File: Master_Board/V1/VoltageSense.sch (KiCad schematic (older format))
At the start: 35 parts, among them J801 649002227222, J802 649002227222, J803 649002227222, J804 649002227222, U801 ACPL-C87A-500E, U802 NCS1S2405SC, U803 ACPL-C87A-500E, U804 LMV321RILT, U805 LMV321RILT

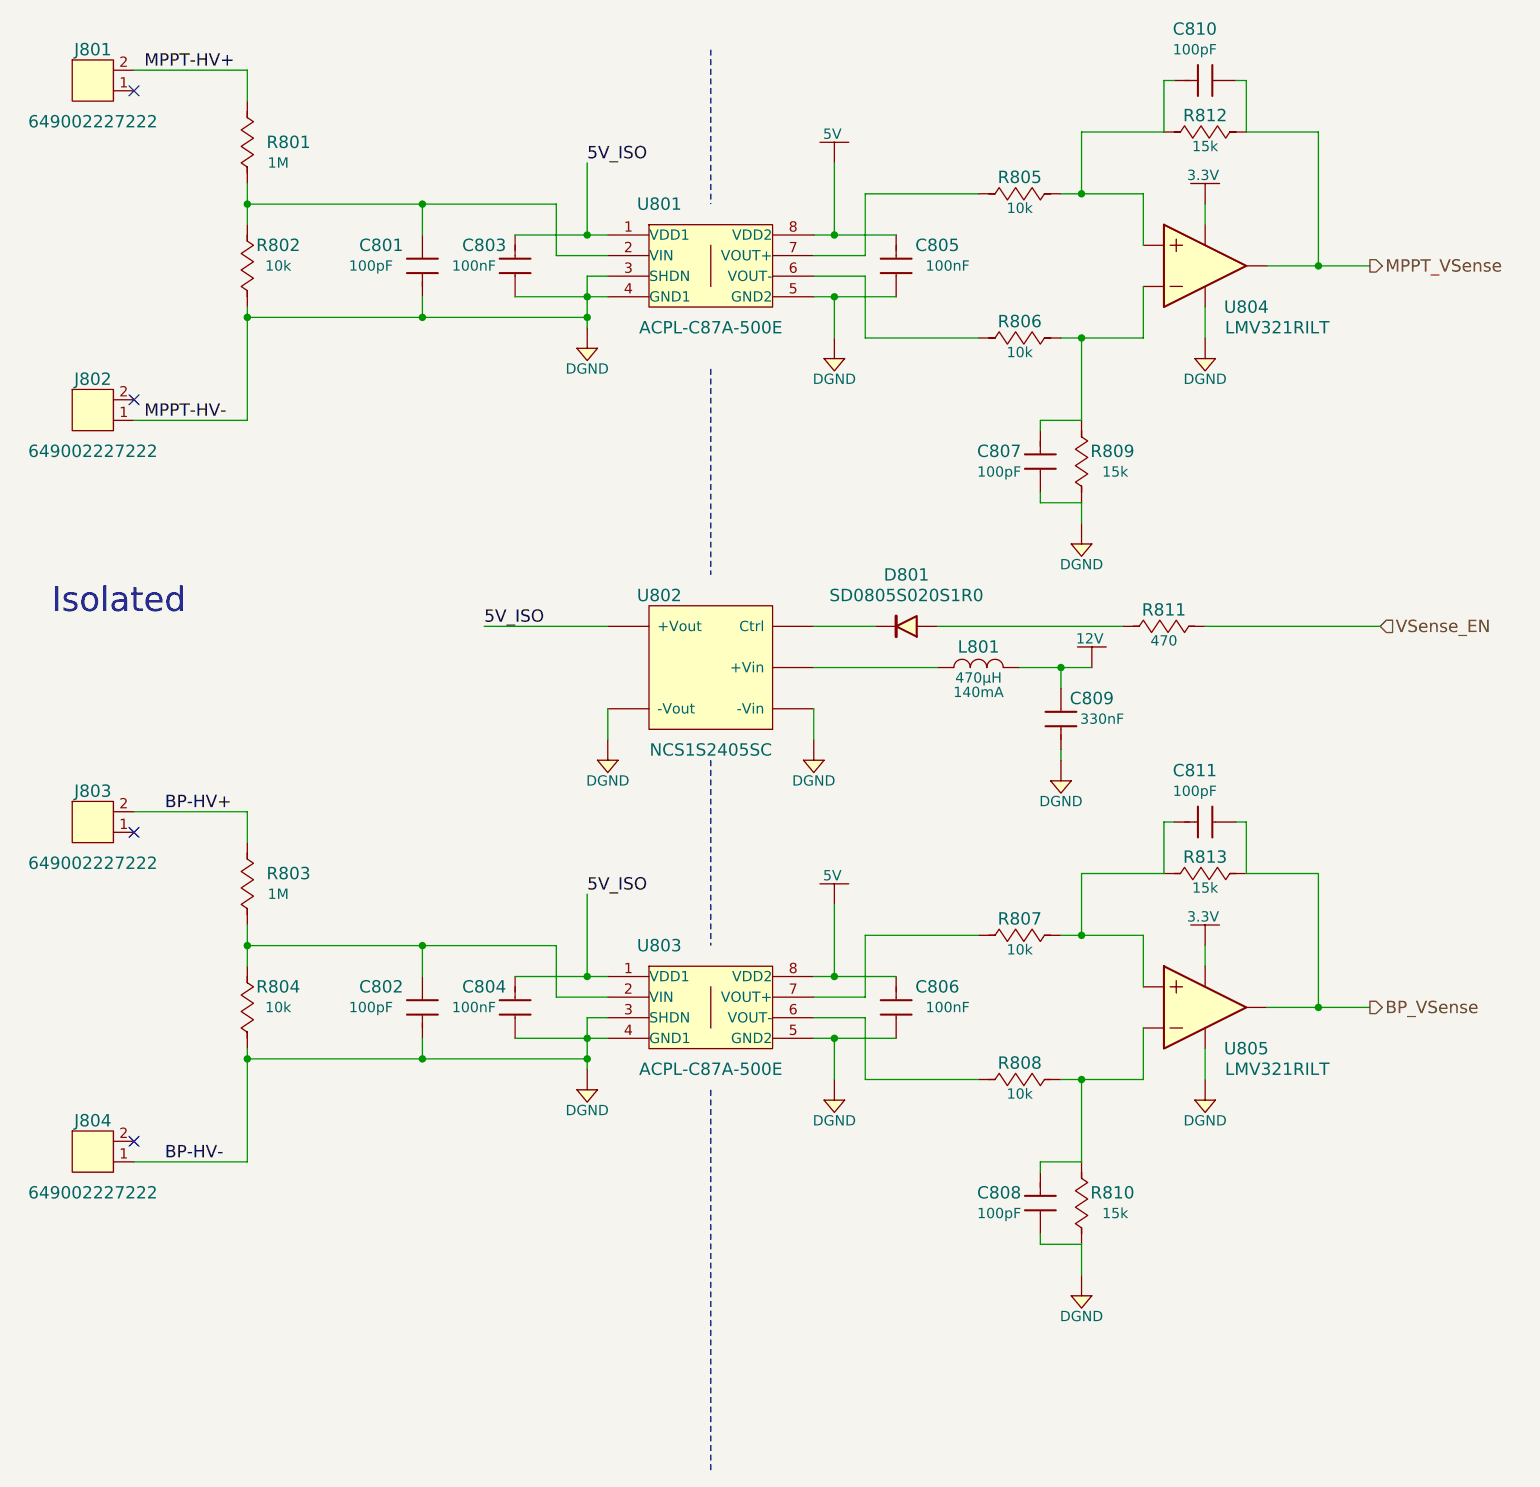
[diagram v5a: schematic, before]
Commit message: Create Master board PCB
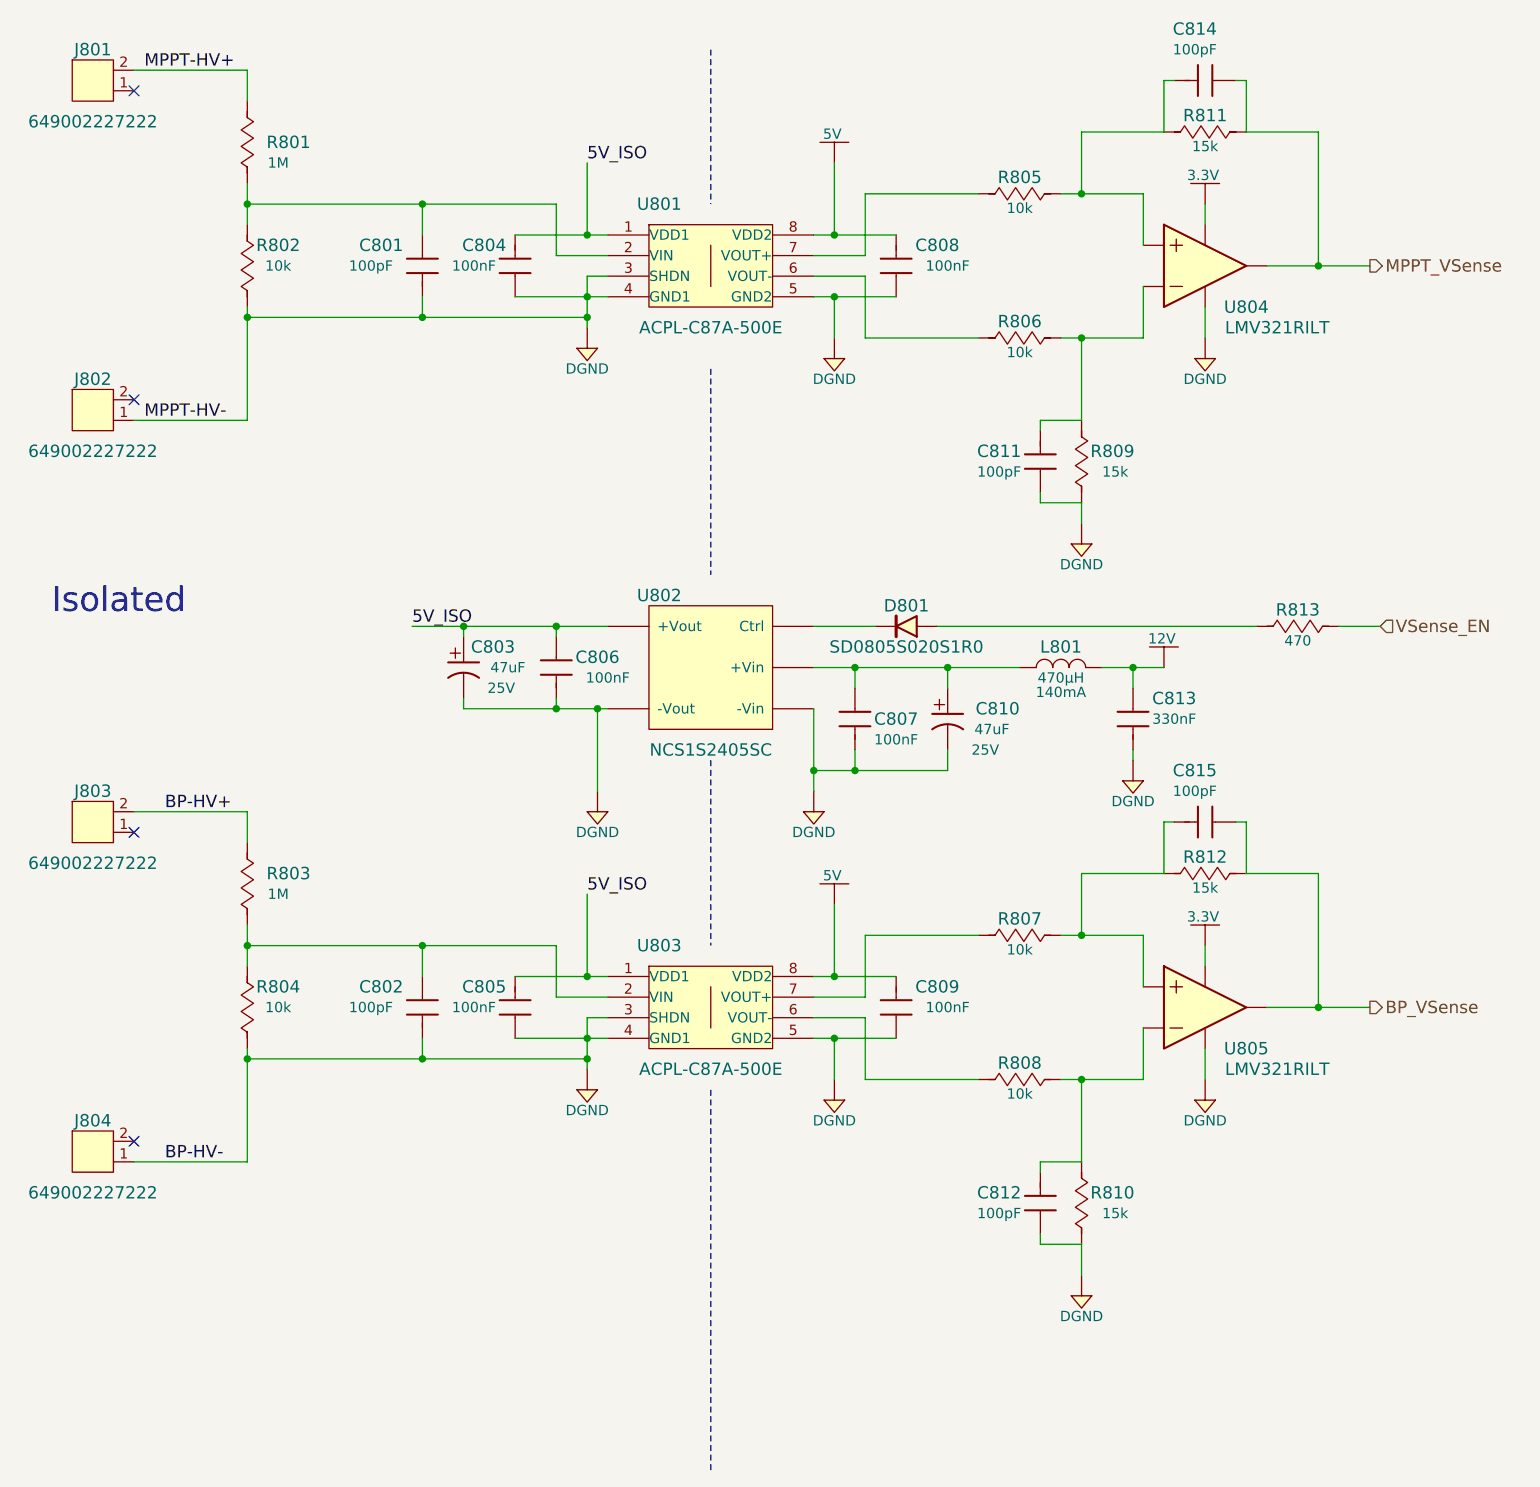
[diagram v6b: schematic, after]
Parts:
- removed L801: RLB0608-471KL, Inductors:RLB0608, symbol RLB0608-471KL
- added C803, C810: 860020472006, Capacitors:Radial-Can-5_11_2, symbol 860020472006
- added C806, C807: 885012207098, Capacitors:C0805, symbol 885012207098
- added L801: 744052471, Inductors:WE-TPC-SMD, symbol 744052471
- renumbered C803 to C804, C804 to C805, C805 to C808, C806 to C809, C807 to C811, C808 to C812, C809 to C813, C810 to C814, C811 to C815, R812 to R811, R813 to R812, R811 to R813
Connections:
- net 12V: now also L801.2
- net 5V_ISO: now also C803.1 (Positif), C806.1
- net DGND: now also C803.2 (Negatif), C806.2, C807.2, C810.2 (Negatif)
- net at U802.2 (+Vin): now also C807.1, C810.1 (Positif), L801.1
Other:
- moved on the sheet: C813, R813

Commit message: Modify Master_board PCB
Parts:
- U802: footprint IC:MSOP-8-EP -> IC:NCS1S2405SC
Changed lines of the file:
@@
 encoding utf-8
 Sheet 8 11
-Title ""
-Date ""
-Rev ""
-Comp ""
-Comment1 ""
+Title "Voltage Sense"
+Date "2017-06-25"
+Rev "V1"
+Comp "Eclipse Solar Car"
+Comment1 "Julien G. Bourassa"
 Comment2 ""
 Comment3 ""
@@
 F 0 "U802" H 5150 3300 60  0000 C CNN
 F 1 "NCS1S2405SC" H 4900 4050 60  0000 C CNN
-F 2 "IC:MSOP-8-EP" H 4950 2600 60  0001 C CNN
+F 2 "IC:NCS1S2405SC" H 4950 2600 60  0001 C CNN
 F 3 "http://power.murata.com/data/power/ncl/kdc_ncs1.pdf" H 4950 2500 60  0001 C CNN
 F 4 "Digikey" H 4900 3100 60  0001 C CNN "Supplier"

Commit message: Routing BmsMasterBoard
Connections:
- net DGND: no longer C801.2, C802.2, C803.2 (Negatif), C804.1, C805.1, C806.2, J802.1, J804.1, R802.2, R804.2, U801.3 (SHDN), U801.4 (GND1), U802.7 (-Vout), U803.3 (SHDN), U803.4 (GND1)
- new net GND: C801.2, C802.2, C803.2 (Negatif), C804.1, C805.1, C806.2, J802.1, J804.1, R802.2, R804.2, U801.3 (SHDN), U801.4 (GND1), U802.7 (-Vout), U803.3 (SHDN), U803.4 (GND1)
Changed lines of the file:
@@
 NoConn ~ 2100 5950
 $Comp
-L DGND #PWR087
-U 1 1 5949C551
-P 4300 5700
-F 0 "#PWR087" H 4300 5530 50  0001 C CNN
-F 1 "DGND" H 4300 5600 50  0000 C CNN
-F 2 "" H 4300 5800 60  0000 C CNN
-F 3 "" H 4280 5610 60  0000 C CNN
-	1    4300 5700
-	1    0    0    -1
-$EndComp
-$Comp
-L DGND #PWR088
+L DGND #PWR084
 U 1 1 5949C56B
 P 5500 5750
-F 0 "#PWR088" H 5500 5580 50  0001 C CNN
+F 0 "#PWR084" H 5500 5580 50  0001 C CNN
 F 1 "DGND" H 5500 5650 50  0000 C CNN
 F 2 "" H 5500 5850 60  0000 C CNN
@@
 BP_VSense
 $Comp
-L DGND #PWR089
+L DGND #PWR085
 U 1 1 5949FCE5
 P 7300 5750
-F 0 "#PWR089" H 7300 5580 50  0001 C CNN
+F 0 "#PWR085" H 7300 5580 50  0001 C CNN
 F 1 "DGND" H 7300 5650 50  0000 C CNN
 F 2 "" H 7300 5850 60  0000 C CNN
@@
 $EndComp
 $Comp
-L DGND #PWR090
+L DGND #PWR086
 U 1 1 594A0EB3
 P 6700 6700
-F 0 "#PWR090" H 6700 6530 50  0001 C CNN
+F 0 "#PWR086" H 6700 6530 50  0001 C CNN
 F 1 "DGND" H 6700 6600 50  0000 C CNN
 F 2 "" H 6700 6800 60  0000 C CNN
@@
 $EndComp
 $Comp
-L 5V #PWR091
+L 5V #PWR087
 U 1 1 594A3B0E
 P 5500 4800
-F 0 "#PWR091" H 5500 4650 50  0001 C CNN
+F 0 "#PWR087" H 5500 4650 50  0001 C CNN
 F 1 "5V" H 5490 4940 50  0000 C CNN
 F 2 "" H 5500 4800 60  0000 C CNN
@@
 $EndComp
 $Comp
-L 3.3V #PWR092
+L 3.3V #PWR088
 U 1 1 594A4CD5
 P 7300 5000
-F 0 "#PWR092" H 7300 4850 50  0001 C CNN
+F 0 "#PWR088" H 7300 4850 50  0001 C CNN
 F 1 "3.3V" H 7290 5140 50  0000 C CNN
 F 2 "" H 7300 5000 60  0000 C CNN
@@
 $EndComp
 $Comp
-L DGND #PWR093
-U 1 1 594A764A
-P 4350 4350
-F 0 "#PWR093" H 4350 4180 50  0001 C CNN
-F 1 "DGND" H 4350 4250 50  0000 C CNN
-F 2 "" H 4350 4450 60  0000 C CNN
-F 3 "" H 4330 4260 60  0000 C CNN
-	1    4350 4350
-	1    0    0    -1
-$EndComp
-$Comp
-L DGND #PWR094
+L DGND #PWR090
 U 1 1 594A76E3
 P 5400 4350
-F 0 "#PWR094" H 5400 4180 50  0001 C CNN
+F 0 "#PWR090" H 5400 4180 50  0001 C CNN
 F 1 "DGND" H 5400 4250 50  0000 C CNN
 F 2 "" H 5400 4450 60  0000 C CNN
@@
 $EndComp
 $Comp
-L 12V #PWR095
+L 12V #PWR091
 U 1 1 594A78A1
 P 7100 3650
-F 0 "#PWR095" H 7100 3500 50  0001 C CNN
+F 0 "#PWR091" H 7100 3500 50  0001 C CNN
 F 1 "12V" H 7090 3790 50  0000 C CNN
 F 2 "" H 7100 3650 60  0000 C CNN
@@
 NoConn ~ 2100 2350
 $Comp
-L DGND #PWR096
-U 1 1 594A898F
-P 4300 2100
-F 0 "#PWR096" H 4300 1930 50  0001 C CNN
-F 1 "DGND" H 4300 2000 50  0000 C CNN
-F 2 "" H 4300 2200 60  0000 C CNN
-F 3 "" H 4280 2010 60  0000 C CNN
-	1    4300 2100
-	1    0    0    -1
-$EndComp
-$Comp
-L DGND #PWR097
+L DGND #PWR093
 U 1 1 594A8995
 P 5500 2150
-F 0 "#PWR097" H 5500 1980 50  0001 C CNN
+F 0 "#PWR093" H 5500 1980 50  0001 C CNN
 F 1 "DGND" H 5500 2050 50  0000 C CNN
 F 2 "" H 5500 2250 60  0000 C CNN
@@
 MPPT_VSense
 $Comp
-L DGND #PWR098
+L DGND #PWR094
 U 1 1 594A8A41
 P 7300 2150
-F 0 "#PWR098" H 7300 1980 50  0001 C CNN
+F 0 "#PWR094" H 7300 1980 50  0001 C CNN
 F 1 "DGND" H 7300 2050 50  0000 C CNN
 F 2 "" H 7300 2250 60  0000 C CNN
@@
 $EndComp
 $Comp
-L DGND #PWR099
+L DGND #PWR095
 U 1 1 594A8A81
 P 6700 3050
-F 0 "#PWR099" H 6700 2880 50  0001 C CNN
+F 0 "#PWR095" H 6700 2880 50  0001 C CNN
 F 1 "DGND" H 6700 2950 50  0000 C CNN
 F 2 "" H 6700 3150 60  0000 C CNN
@@
 $EndComp
 $Comp
-L 5V #PWR0100
+L 5V #PWR096
 U 1 1 594A8A88
 P 5500 1200
-F 0 "#PWR0100" H 5500 1050 50  0001 C CNN
+F 0 "#PWR096" H 5500 1050 50  0001 C CNN
 F 1 "5V" H 5490 1340 50  0000 C CNN
 F 2 "" H 5500 1200 60  0000 C CNN
@@
 $EndComp
 $Comp
-L 3.3V #PWR0101
+L 3.3V #PWR097
 U 1 1 594A8A8E
 P 7300 1400
-F 0 "#PWR0101" H 7300 1250 50  0001 C CNN
+F 0 "#PWR097" H 7300 1250 50  0001 C CNN
 F 1 "3.3V" H 7290 1540 50  0000 C CNN
 F 2 "" H 7300 1400 60  0000 C CNN
@@
 	6800 3650 7100 3650
 $Comp
-L DGND #PWR0102
+L DGND #PWR098
 U 1 1 59486B2F
 P 6950 4200
-F 0 "#PWR0102" H 6950 4030 50  0001 C CNN
+F 0 "#PWR098" H 6950 4030 50  0001 C CNN
 F 1 "DGND" H 6950 4100 50  0000 C CNN
 F 2 "" H 6950 4300 60  0000 C CNN
@@
 	1    0    0    -1
 $EndComp
+$Comp
+L GND #PWR?
+U 1 1 595310B3
+P 4300 2100
+F 0 "#PWR?" H 4300 1930 50  0001 C CNN
+F 1 "GND" H 4300 2000 50  0000 C CNN
+F 2 "" H 4300 2200 60  0000 C CNN
+F 3 "" H 4280 2010 60  0000 C CNN
+	1    4300 2100
+	1    0    0    -1
+$EndComp
+$Comp
+L GND #PWR?
+U 1 1 595314E7
+P 4350 4350
+F 0 "#PWR?" H 4350 4180 50  0001 C CNN
+F 1 "GND" H 4350 4250 50  0000 C CNN
+F 2 "" H 4350 4450 60  0000 C CNN
+F 3 "" H 4330 4260 60  0000 C CNN
+	1    4350 4350
+	1    0    0    -1
+$EndComp
+$Comp
+L GND #PWR?
+U 1 1 59531ABC
+P 4300 5700
+F 0 "#PWR?" H 4300 5530 50  0001 C CNN
+F 1 "GND" H 4300 5600 50  0000 C CNN
+F 2 "" H 4300 5800 60  0000 C CNN
+F 3 "" H 4280 5610 60  0000 C CNN
+	1    4300 5700
+	1    0    0    -1
+$EndComp
